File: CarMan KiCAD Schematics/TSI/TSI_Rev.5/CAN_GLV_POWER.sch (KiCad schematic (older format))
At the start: 35 parts, among them Q11 TN2130K1-G, U14 MountingHole, U15 MountingHole, U17 ChassisGND, U2 SFS2-DC24V, U24 TLP293, U28 MountingHole, U33 SFS2-DC24V, U41 PDQ10-Q24-D5-D, U42 LT1763CS8-3.3PBF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

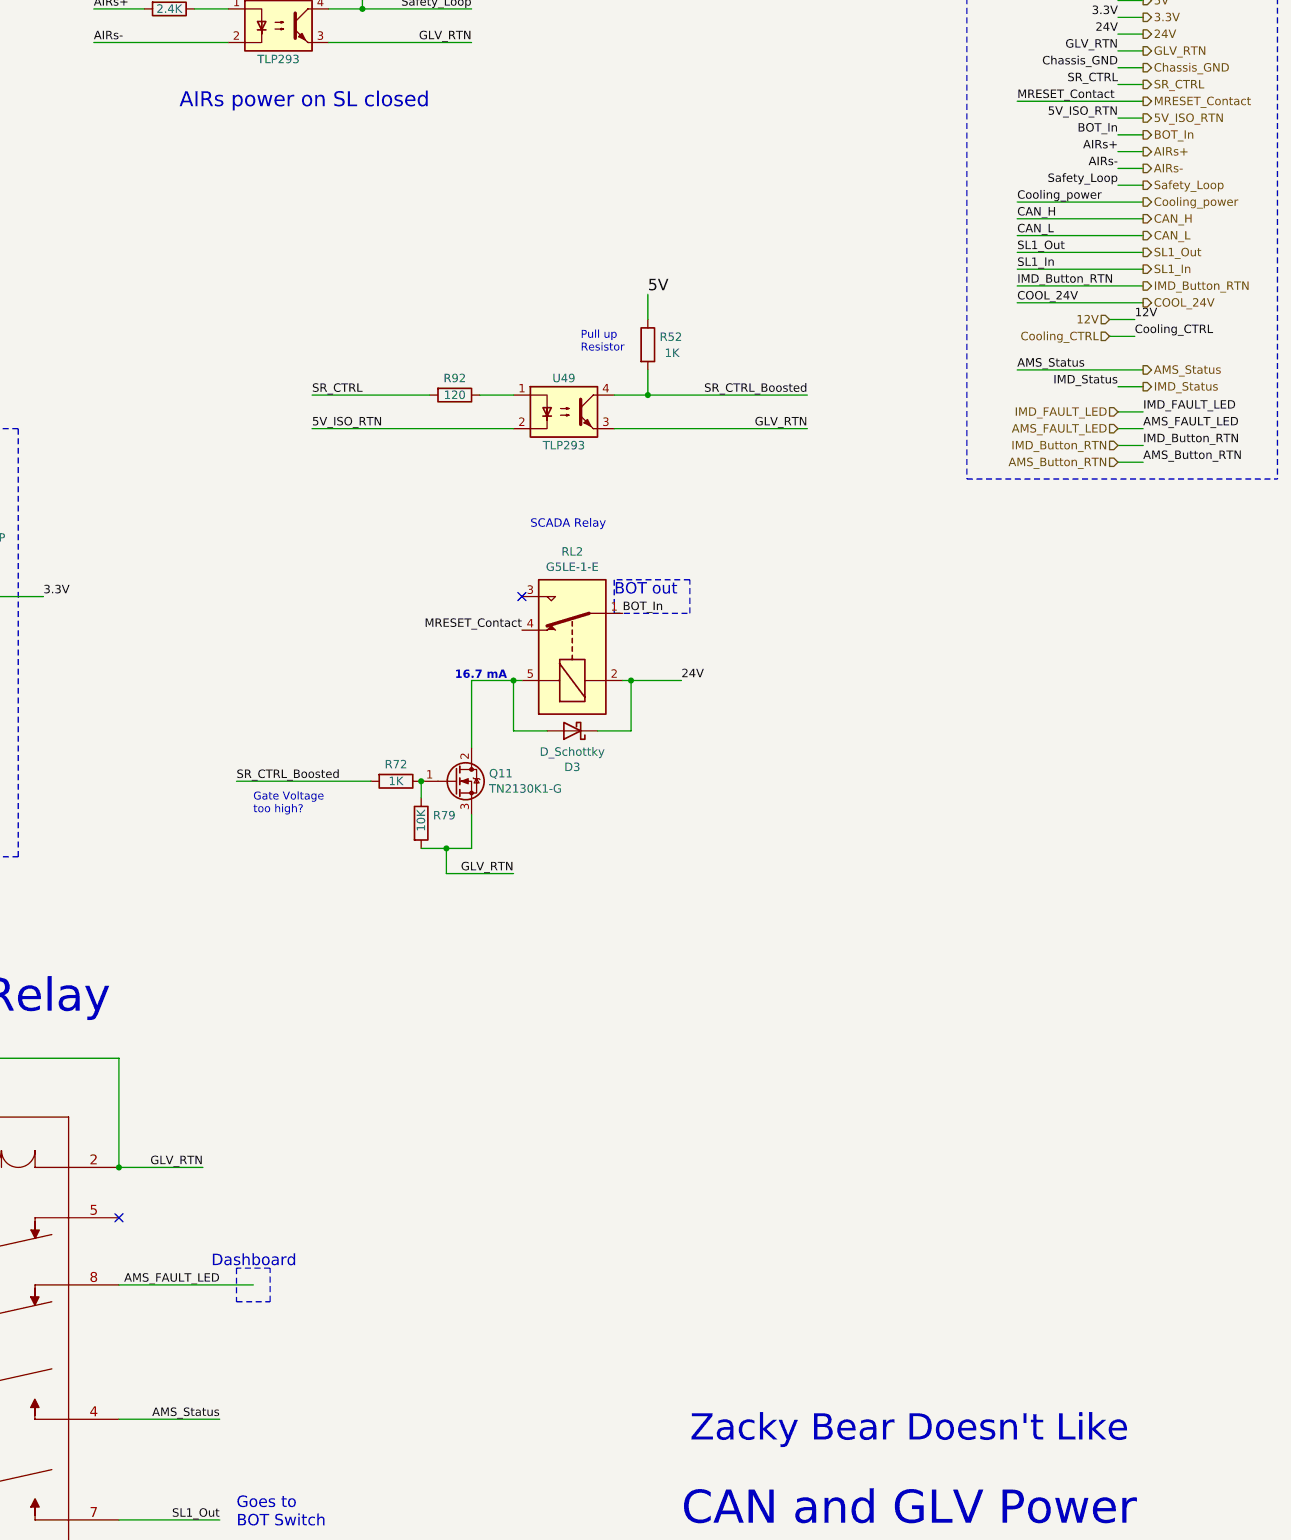
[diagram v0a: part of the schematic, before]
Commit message: - Aesthetics - TSI Safety Loop Edits - Battery pack connection editing
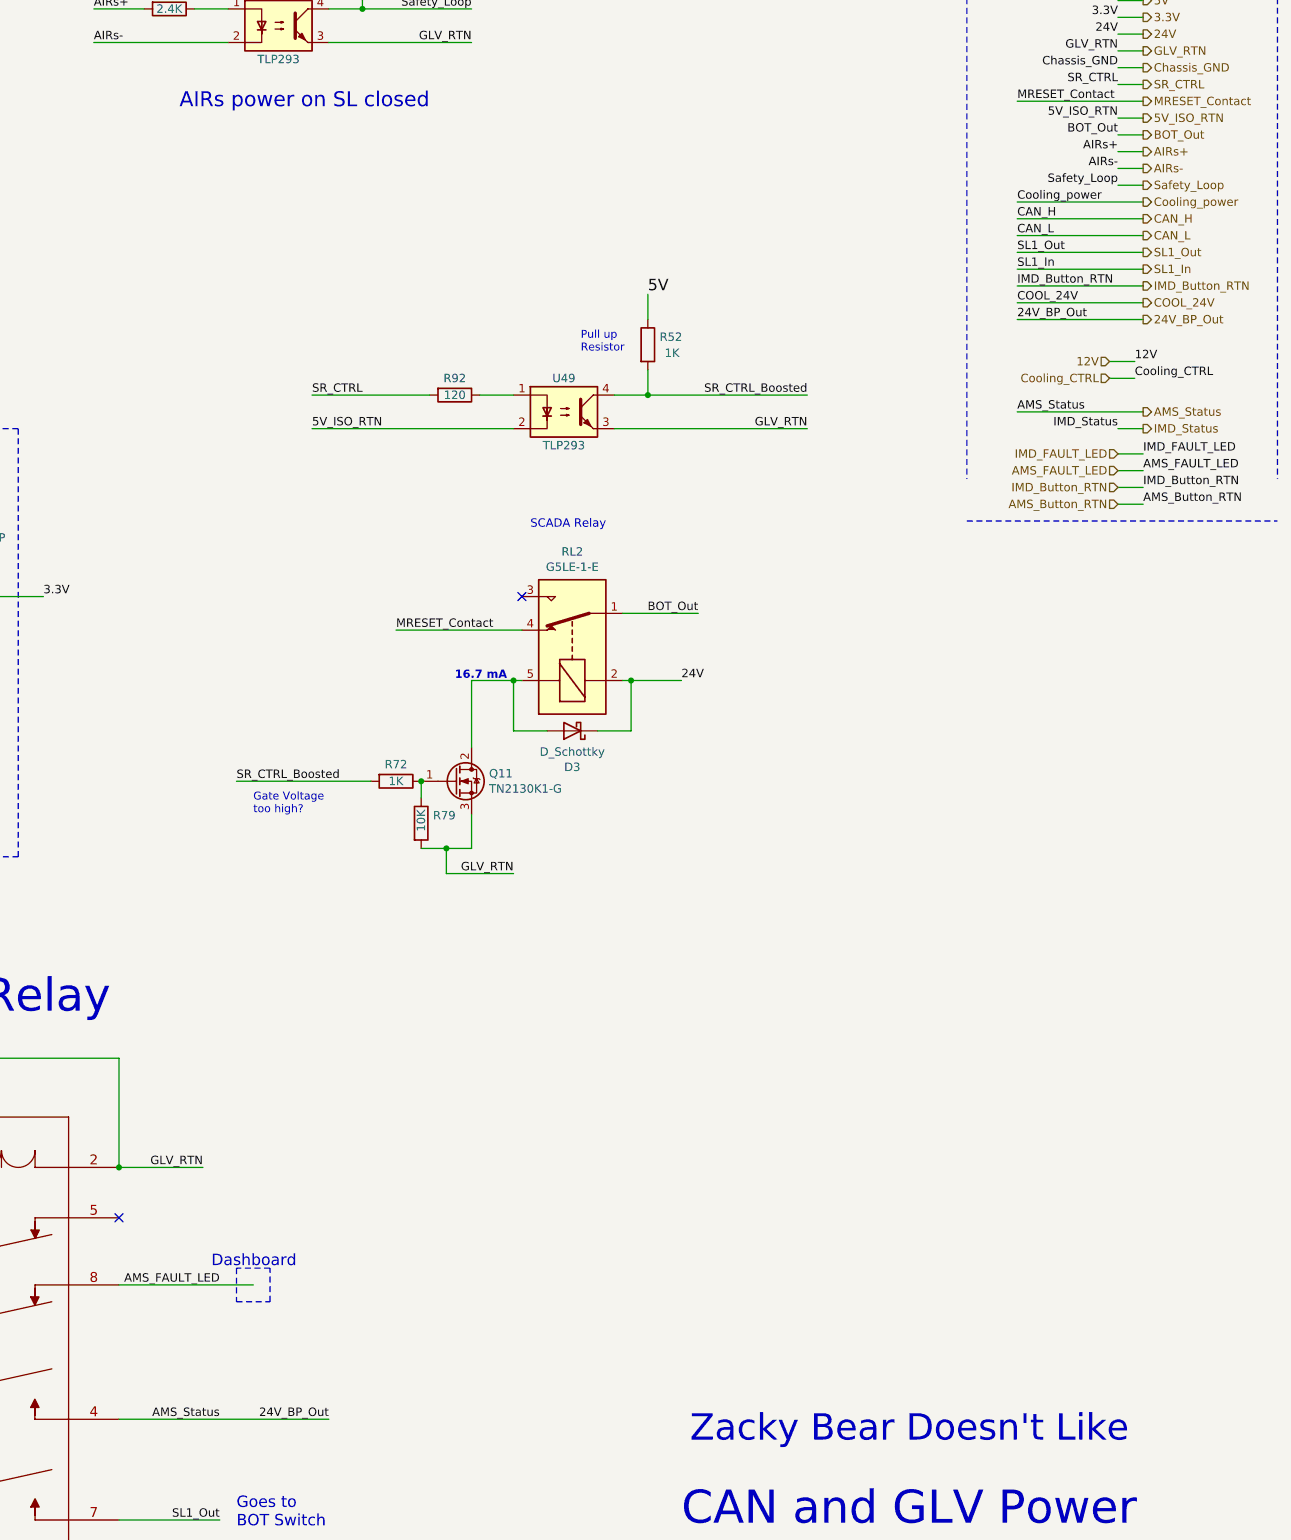
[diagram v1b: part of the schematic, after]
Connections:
- net labels added: 24V_BP_Out, BOT_Out
- net labels removed: BOT_In
- wire segments 176 -> 179
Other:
- note removed: "\nBOT out"
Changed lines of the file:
@@
 Text Notes 12450 10350 0    197  ~ 0
 CAN and GLV Power
-$Comp
-L TSI_Rev.5-rescue:G5LE-1-E-Lafayette_Electric_Car_Internals RL?
-U 1 1 5FB466B1
-P 11800 5100
-AR Path="/5FB466B1" Ref="RL?"  Part="1"
-AR Path="/5FE1DE7D/5FB466B1" Ref="RL2"  Part="1"
-F 0 "RL2" V 12367 5100 50  0000 C CNN
-F 1 "G5LE-1-E" V 12276 5100 50  0000 C CNN
-F 2 "" H 12050 5700 50  0001 C CNN
-F 3 "https://media.digikey.com/pdf/Data%20Sheets/Omron%20PDFs/G5LE-E_G.pdf" H 12050 5700 50  0001 C CNN
-	1    11800 5100
-	0    -1   -1   0
-$EndComp
 Text Label 10250 3600 0    50   ~ 0
 SR_CTRL
@@
 Wire Wire Line
 	12100 5300 12150 5300
-Text Label 12100 4900 0    50   ~ 0
-BOT_In
 NoConn ~ 11500 4800
 Text Notes 14800 750  0    98   ~ 0
 SIGNALS
 Wire Notes Line
-	14150 4100 16000 4100
+	14150 4350 16000 4350
 Wire Notes Line
 	16000 550  14150 550
@@
 Text Label 1900 2850 0    50   ~ 0
 Cooling_power
-Text Label 11500 5000 2    50   ~ 0
+Text Label 10750 5000 0    50   ~ 0
 MRESET_Contact
 Text Notes 5400 1050 2    89   ~ 0
@@
 $EndComp
 Text Label 15050 2050 2    50   ~ 0
-BOT_In
+BOT_Out
 Wire Wire Line
 	15200 2050 15050 2050
 Text HLabel 15200 2050 2    50   Output ~ 0
-BOT_In
+BOT_Out
 Text Label 15050 1950 2    50   ~ 0
 5V_ISO_RTN
@@
 Text HLabel 15200 2450 2    50   Output ~ 0
 Cooling_power
-Text Label 15050 3550 2    50   ~ 0
+Text Label 15050 3800 2    50   ~ 0
 IMD_Status
 Text Label 15050 2350 2    50   ~ 0
 Safety_Loop
 Wire Wire Line
-	15200 3550 15050 3550
+	15200 3800 15050 3800
 Wire Wire Line
 	15200 2350 15050 2350
-Text HLabel 15200 3550 2    50   Output ~ 0
+Text HLabel 15200 3800 2    50   Output ~ 0
 IMD_Status
 Text HLabel 15200 2350 2    50   Output ~ 0
@@
 Text Notes 4650 8850 0    68   ~ 0
 Dashboard\n
-Text HLabel 15200 3450 2    50   Output ~ 0
+Text HLabel 15200 3700 2    50   Output ~ 0
 AMS_Status
-Text Label 14450 3450 0    50   ~ 0
+Text Label 14450 3700 0    50   ~ 0
 AMS_Status
 Text Label 14450 2950 0    50   ~ 0
@@
 	14450 2850 15200 2850
 Wire Wire Line
-	14450 3450 15200 3450
+	14450 3700 15200 3700
 Wire Wire Line
 	14450 3050 15200 3050
@@
 	14450 2750 15200 2750
 Wire Wire Line
-	15200 3700 15050 3700
-Text HLabel 15050 3700 0    50   Input ~ 0
+	15200 3950 15050 3950
+Text HLabel 15050 3950 0    50   Input ~ 0
 IMD_FAULT_LED
-Text Label 15200 3700 0    50   ~ 0
+Text Label 15200 3950 0    50   ~ 0
 IMD_FAULT_LED
 Wire Wire Line
-	15150 3150 15000 3150
-Text HLabel 15000 3150 0    50   Input ~ 0
+	15150 3400 15000 3400
+Text HLabel 15000 3400 0    50   Input ~ 0
 12V
-Text Label 15150 3150 0    50   ~ 0
+Text Label 15150 3400 0    50   ~ 0
 12V
 Wire Wire Line
-	15150 3250 15000 3250
-Text HLabel 15000 3250 0    50   Input ~ 0
+	15150 3500 15000 3500
+Text HLabel 15000 3500 0    50   Input ~ 0
 Cooling_CTRL
-Text Label 15150 3250 0    50   ~ 0
+Text Label 15150 3500 0    50   ~ 0
 Cooling_CTRL
 Wire Wire Line
-	15200 3900 15050 3900
-Text HLabel 15050 3900 0    50   Input ~ 0
+	15200 4150 15050 4150
+Text HLabel 15050 4150 0    50   Input ~ 0
 IMD_Button_RTN
-Text Label 15200 3900 0    50   ~ 0
+Text Label 15200 4150 0    50   ~ 0
 IMD_Button_RTN
 Wire Wire Line
-	15200 4000 15050 4000
-Text HLabel 15050 4000 0    50   Input ~ 0
+	15200 4250 15050 4250
+Text HLabel 15050 4250 0    50   Input ~ 0
 AMS_Button_RTN
-Text Label 15200 4000 0    50   ~ 0
+Text Label 15200 4250 0    50   ~ 0
 AMS_Button_RTN
 Wire Notes Line
@@
 	14150 550  14150 4100
 Wire Wire Line
-	15200 3800 15050 3800
-Text HLabel 15050 3800 0    50   Input ~ 0
+	15200 4050 15050 4050
+Text HLabel 15050 4050 0    50   Input ~ 0
 AMS_FAULT_LED
-Text Label 15200 3800 0    50   ~ 0
+Text Label 15200 4050 0    50   ~ 0
 AMS_FAULT_LED
 Text Label 9600 8200 2    50   ~ 0
@@
 AMS_Status
 Wire Wire Line
-	9700 9700 9100 9700
-Wire Wire Line
 	6250 9600 7300 9600
 Text Label 5550 8800 0    50   ~ 0
@@
 Text Notes 9800 10350 0    68   ~ 0
 Goes to \nBOT Switch
-Wire Wire Line
-	7300 9200 6700 9200
-Text Label 6700 9200 0    50   ~ 0
-24V
 Text Label 9700 8900 2    50   ~ 0
 AMS_FAULT_LED
@@
 Wire Wire Line
 	7300 10900 8200 10900
-Text Notes 12050 4800 0    68   ~ 0
-\nBOT out
-Wire Notes Line
-	12050 4700 12050 4900
-Wire Notes Line
-	12050 4900 12500 4900
-Wire Notes Line
-	12500 4900 12500 4700
-Wire Notes Line
-	12500 4700 12050 4700
+$Comp
+L TSI_Rev.5-rescue:G5LE-1-E-Lafayette_Electric_Car_Internals RL?
+U 1 1 5FB466B1
+P 11800 5100
+AR Path="/5FB466B1" Ref="RL?"  Part="1"
+AR Path="/5FE1DE7D/5FB466B1" Ref="RL2"  Part="1"
+F 0 "RL2" V 12367 5100 50  0000 C CNN
+F 1 "G5LE-1-E" V 12276 5100 50  0000 C CNN
+F 2 "" H 12050 5700 50  0001 C CNN
+F 3 "https://media.digikey.com/pdf/Data%20Sheets/Omron%20PDFs/G5LE-E_G.pdf" H 12050 5700 50  0001 C CNN
+	1    11800 5100
+	0    -1   -1   0
+$EndComp
+Wire Wire Line
+	12550 4900 12100 4900
+Text Label 12550 4900 2    50   ~ 0
+BOT_Out
+Wire Wire Line
+	10750 5000 11500 5000
+Wire Wire Line
+	7300 9200 6700 9200
+Text Label 6700 9200 0    50   ~ 0
+24V
+Text HLabel 15200 3150 2    50   Output ~ 0
+24V_BP_Out
+Wire Wire Line
+	14450 3150 15200 3150
+Text Label 14450 3150 0    50   ~ 0
+24V_BP_Out
+Text Label 10350 9700 2    50   ~ 0
+24V_BP_Out
+Wire Wire Line
+	9100 9700 10350 9700
 $EndSCHEMATC

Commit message: Smol Edits
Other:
- note added: "Control Signal used as a \npsuedo relay"
- moved on the sheet: C13, C18, PS2, R57, R71, U48
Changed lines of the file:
@@
 L Device:R R71
 U 1 1 5FA34D6C
-P 4150 1400
-F 0 "R71" V 4050 1400 50  0000 C CNN
-F 1 "2.1K" V 4150 1400 50  0000 C CNN
-F 2 "" V 4080 1400 50  0001 C CNN
-F 3 "~" H 4150 1400 50  0001 C CNN
-	1    4150 1400
+P 4000 1050
+F 0 "R71" V 3900 1050 50  0000 C CNN
+F 1 "2.1K" V 4000 1050 50  0000 C CNN
+F 2 "" V 3930 1050 50  0001 C CNN
+F 3 "~" H 4000 1050 50  0001 C CNN
+	1    4000 1050
 	0    1    1    0
 $EndComp
 Wire Wire Line
-	4500 1400 4300 1400
-Text Label 3500 1400 0    50   ~ 0
+	4350 1050 4150 1050
+Text Label 3350 1050 0    50   ~ 0
 Cooling_CTRL
 $Comp
 L TSI_Rev.5-rescue:TLP293-CarMan_KiCAD_Library-TSI_Rev.5-rescue U48
 U 1 1 5FA22056
-P 4800 1500
-F 0 "U48" H 4800 1700 50  0000 C CNN
-F 1 "TLP293" H 4800 1300 50  0000 C CNN
-F 2 "Package_SO:SOIC-4_4.55x2.6mm_P1.27mm" H 4600 1300 50  0001 L CIN
-F 3 "" H 4800 1500 50  0001 L CNN
-	1    4800 1500
-	1    0    0    -1
-$EndComp
-Text Label 3500 1600 0    50   ~ 0
+P 4650 1150
+F 0 "U48" H 4650 1350 50  0000 C CNN
+F 1 "TLP293" H 4650 950 50  0000 C CNN
+F 2 "Package_SO:SOIC-4_4.55x2.6mm_P1.27mm" H 4450 950 50  0001 L CIN
+F 3 "" H 4650 1150 50  0001 L CNN
+	1    4650 1150
+	1    0    0    -1
+$EndComp
+Text Label 3350 1250 0    50   ~ 0
 5V_ISO_RTN
-Text Label 1900 2850 0    50   ~ 0
-Cooling_power
 Text Label 10750 5000 0    50   ~ 0
 MRESET_Contact
-Text Notes 5400 1050 2    89   ~ 0
+Text Notes 5250 800  2    89   ~ 0
 Cooling Control\n
 $Comp
@@
 Text Notes 12500 9850 0    157  ~ 0
 Zacky Bear Doesn't Like
-$Comp
-L CarMan_KiCAD_Library:EHHD010A0B41-HZ PS2
-U 1 1 5FB4FED7
-P 3050 3050
-F 0 "PS2" H 3050 3717 50  0000 C CNN
-F 1 "EHHD010A0B41-HZ" H 3050 3626 50  0000 C CNN
-F 2 "CONV_EHHD010A0B41-HZ" H 3050 3050 50  0001 L BNN
-F 3 "https://library.industrialsolutions.abb.com/publibrary/checkout/DS-EHHD010A0B?TNR=Data%20Sheets|DS-EHHD010A0B|PDF" H 3050 3050 50  0001 L BNN
-F 4 "Manufacturer Recommendations" H 3050 3050 50  0001 L BNN "STANDARD"
-F 5 "April 6, 2016" H 3050 3050 50  0001 L BNN "PARTREV"
-F 6 "GE" H 3050 3050 50  0001 L BNN "MANUFACTURER"
-F 7 "12.7mm" H 3050 3050 50  0001 L BNN "MAXIMUM_PACKAGE_HEIGHT"
-	1    3050 3050
-	1    0    0    -1
-$EndComp
-$Comp
-L Device:C C13
-U 1 1 5FB58791
-P 1450 2800
-F 0 "C13" H 1565 2846 50  0000 L CNN
-F 1 "100u" H 1565 2755 50  0000 L CNN
-F 2 "" H 1488 2650 50  0001 C CNN
-F 3 "~" H 1450 2800 50  0001 C CNN
-	1    1450 2800
-	1    0    0    -1
-$EndComp
-$Comp
-L Device:C C18
-U 1 1 5FB588C1
-P 4050 2800
-F 0 "C18" H 4165 2846 50  0000 L CNN
-F 1 "10u" H 4165 2755 50  0000 L CNN
-F 2 "" H 4088 2650 50  0001 C CNN
-F 3 "~" H 4050 2800 50  0001 C CNN
-	1    4050 2800
-	1    0    0    -1
-$EndComp
-Connection ~ 1450 2650
-Wire Wire Line
-	1450 2950 1450 3050
-Connection ~ 1450 3050
-Wire Wire Line
-	650  2650 1450 2650
-Wire Wire Line
-	650  3050 1450 3050
-NoConn ~ 2450 3250
-NoConn ~ 2450 3350
-NoConn ~ 3650 2850
-Wire Wire Line
-	3650 3050 3650 3550
-Wire Wire Line
-	3650 3550 2350 3550
-Wire Wire Line
-	2350 3550 2350 3050
-Wire Wire Line
-	2350 3050 2450 3050
-Wire Wire Line
-	3650 2650 3850 2650
-Wire Wire Line
-	4050 2950 4050 3050
-Wire Wire Line
-	4050 3050 3650 3050
-Connection ~ 3650 3050
-Text Label 650  2650 0    49   ~ 0
-COOL_24V
-Text Label 650  3050 0    49   ~ 0
-GLV_RTN
-Text Label 4450 2650 2    49   ~ 0
+Text Label 7050 2250 2    49   ~ 0
 12V
-$Comp
-L power:PWR_FLAG #FLG02
-U 1 1 5FBAC9F1
-P 3850 2650
-F 0 "#FLG02" H 3850 2725 50  0001 C CNN
-F 1 "PWR_FLAG" H 3850 2823 50  0000 C CNN
-F 2 "" H 3850 2650 50  0001 C CNN
-F 3 "~" H 3850 2650 50  0001 C CNN
-	1    3850 2650
-	1    0    0    -1
-$EndComp
-Connection ~ 3850 2650
-Wire Wire Line
-	3850 2650 4050 2650
-Text Notes 2550 2250 0    49   ~ 0
-DC/DC Converter 24V to 12V 10A
 Wire Wire Line
 	3650 4700 4350 4700
@@
 	1    0    0    -1
 $EndComp
-Wire Wire Line
-	1450 3050 2350 3050
-Connection ~ 2350 3050
-Wire Wire Line
-	1450 2650 2450 2650
 Text Notes 10950 1900 2    89   ~ 0
 AIRs power on SL closed
@@
 	10250 3600 10950 3600
 Wire Wire Line
-	3500 1400 4000 1400
-Wire Wire Line
-	3500 1600 4500 1600
+	3350 1050 3850 1050
+Wire Wire Line
+	3350 1250 4350 1250
 Text Notes 11850 3350 0    47   ~ 0
 Pull up \nResistor
-Wire Wire Line
-	1900 2850 2450 2850
 $Comp
 L Device:R R57
 U 1 1 5FD164DD
-P 5350 1800
-F 0 "R57" H 5420 1846 50  0000 L CNN
-F 1 "40K" H 5420 1755 50  0000 L CNN
-F 2 "" V 5280 1800 50  0001 C CNN
-F 3 "~" H 5350 1800 50  0001 C CNN
-	1    5350 1800
+P 5200 1450
+F 0 "R57" H 5270 1496 50  0000 L CNN
+F 1 "40K" H 5270 1405 50  0000 L CNN
+F 2 "" V 5130 1450 50  0001 C CNN
+F 3 "~" H 5200 1450 50  0001 C CNN
+	1    5200 1450
 	-1   0    0    1
 $EndComp
 Wire Wire Line
-	5350 2050 5350 1950
-Wire Wire Line
-	5100 1600 5350 1600
-Wire Wire Line
-	5350 1600 5350 1650
-Connection ~ 5350 1600
-Wire Wire Line
-	5350 1600 6050 1600
-Text Label 6050 1400 2    50   ~ 0
+	5200 1700 5200 1600
+Wire Wire Line
+	4950 1250 5200 1250
+Wire Wire Line
+	5200 1250 5200 1300
+Connection ~ 5200 1250
+Wire Wire Line
+	5200 1250 5900 1250
+Text Label 5900 1050 2    50   ~ 0
 5V
-Text Label 6050 1600 2    50   ~ 0
+Text Label 5900 1250 2    50   ~ 0
 Cooling_power
-Text Label 5350 2050 0    47   ~ 0
-GLV_RTN
-Wire Wire Line
-	5100 1400 6050 1400
-Wire Wire Line
-	4450 2650 4050 2650
-Connection ~ 4050 2650
+Text Label 5200 1700 0    47   ~ 0
+GLV_RTN
+Wire Wire Line
+	4950 1050 5900 1050
 Wire Wire Line
 	10350 1500 11200 1500
@@
 Wire Wire Line
 	9100 9700 10350 9700
+Text Label 3250 5500 2    50   ~ 0
+GLV_RTN
+Connection ~ 6650 2250
+Wire Wire Line
+	7050 2250 6650 2250
+Wire Wire Line
+	4500 2450 5050 2450
+Wire Wire Line
+	4050 2250 5050 2250
+Connection ~ 4950 2650
+Wire Wire Line
+	4050 2650 4950 2650
+Text Notes 3700 2050 0    49   ~ 0
+DC/DC Converter 24V to 12V 10A
+Wire Wire Line
+	6450 2250 6650 2250
+Connection ~ 6450 2250
+$Comp
+L power:PWR_FLAG #FLG02
+U 1 1 5FBAC9F1
+P 6450 2250
+F 0 "#FLG02" H 6450 2325 50  0001 C CNN
+F 1 "PWR_FLAG" H 6450 2423 50  0000 C CNN
+F 2 "" H 6450 2250 50  0001 C CNN
+F 3 "~" H 6450 2250 50  0001 C CNN
+	1    6450 2250
+	1    0    0    -1
+$EndComp
+Text Label 3250 2650 0    49   ~ 0
+GLV_RTN
+Text Label 3250 2250 0    49   ~ 0
+COOL_24V
+Connection ~ 6250 2650
+Wire Wire Line
+	6650 2650 6250 2650
+Wire Wire Line
+	6650 2550 6650 2650
+Wire Wire Line
+	6250 2250 6450 2250
+Wire Wire Line
+	4950 2650 5050 2650
+Wire Wire Line
+	4950 3150 4950 2650
+Wire Wire Line
+	6250 3150 4950 3150
+Wire Wire Line
+	6250 2650 6250 3150
+NoConn ~ 6250 2450
+NoConn ~ 5050 2950
+NoConn ~ 5050 2850
+Wire Wire Line
+	3250 2650 4050 2650
+Wire Wire Line
+	3250 2250 4050 2250
+Connection ~ 4050 2650
+Wire Wire Line
+	4050 2550 4050 2650
+Connection ~ 4050 2250
+$Comp
+L Device:C C18
+U 1 1 5FB588C1
+P 6650 2400
+F 0 "C18" H 6765 2446 50  0000 L CNN
+F 1 "10u" H 6765 2355 50  0000 L CNN
+F 2 "" H 6688 2250 50  0001 C CNN
+F 3 "~" H 6650 2400 50  0001 C CNN
+	1    6650 2400
+	1    0    0    -1
+$EndComp
+$Comp
+L Device:C C13
+U 1 1 5FB58791
+P 4050 2400
+F 0 "C13" H 4165 2446 50  0000 L CNN
+F 1 "100u" H 4165 2355 50  0000 L CNN
+F 2 "" H 4088 2250 50  0001 C CNN
+F 3 "~" H 4050 2400 50  0001 C CNN
+	1    4050 2400
+	1    0    0    -1
+$EndComp
+$Comp
+L CarMan_KiCAD_Library:EHHD010A0B41-HZ PS2
+U 1 1 5FB4FED7
+P 5650 2650
+F 0 "PS2" H 5650 3317 50  0000 C CNN
+F 1 "EHHD010A0B41-HZ" H 5650 3226 50  0000 C CNN
+F 2 "CONV_EHHD010A0B41-HZ" H 5650 2650 50  0001 L BNN
+F 3 "https://library.industrialsolutions.abb.com/publibrary/checkout/DS-EHHD010A0B?TNR=Data%20Sheets|DS-EHHD010A0B|PDF" H 5650 2650 50  0001 L BNN
+F 4 "Manufacturer Recommendations" H 5650 2650 50  0001 L BNN "STANDARD"
+F 5 "April 6, 2016" H 5650 2650 50  0001 L BNN "PARTREV"
+F 6 "GE" H 5650 2650 50  0001 L BNN "MANUFACTURER"
+F 7 "12.7mm" H 5650 2650 50  0001 L BNN "MAXIMUM_PACKAGE_HEIGHT"
+	1    5650 2650
+	1    0    0    -1
+$EndComp
+Text Label 4500 2450 0    50   ~ 0
+Cooling_power
+Wire Notes Line
+	2950 3250 7450 3250
+Wire Notes Line
+	7450 3250 7450 650
+Wire Notes Line
+	7450 650  2950 650
+Wire Notes Line
+	2950 650  2950 3250
+Text Notes 3650 3000 0    55   ~ 0
+Control Signal used as a \npsuedo relay
 $EndSCHEMATC
